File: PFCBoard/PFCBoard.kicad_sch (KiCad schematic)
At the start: 17 parts, among them J1 VIN 10-30VDC, J2 Coin Out, U1 NE555D, U2 MC78L05_SOT89, U3 LTV-817S

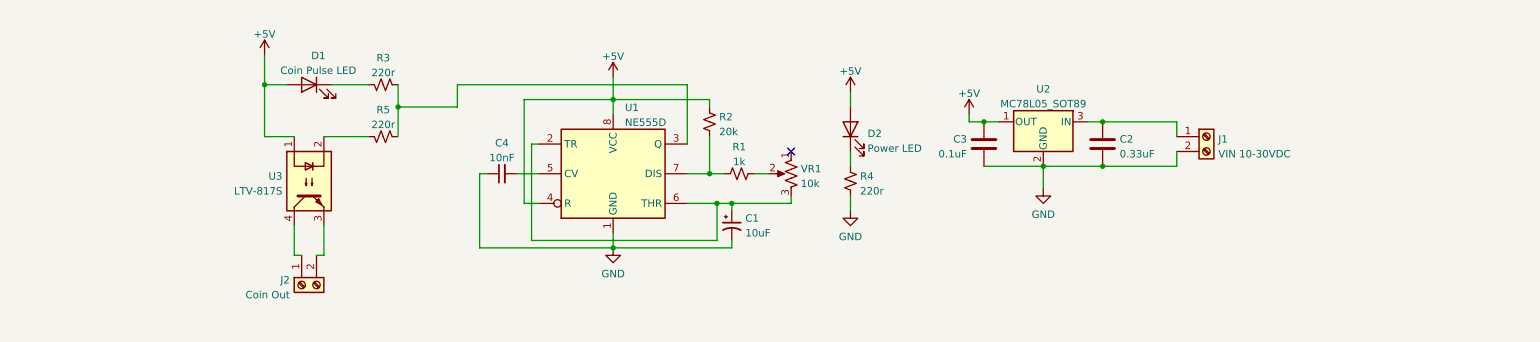
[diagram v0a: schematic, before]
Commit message: Add voltage selection, pre-rendered schematic
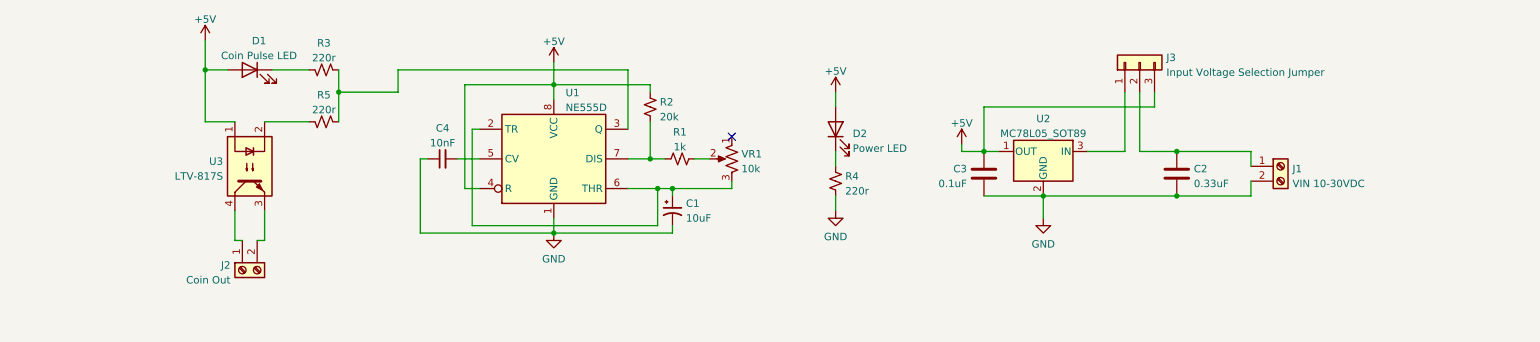
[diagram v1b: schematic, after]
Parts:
- added J3: Input Voltage Selection Jumper, symbol Connector_Generic:Conn_01x03
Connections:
- net +5V: now also J3.3 (Pin_3)
- net at C2.1, J1.1 (Pin_1): now also J3.2 (Pin_2); no longer U2.3 (IN)
- new net: J3.1 (Pin_1), U2.3 (IN)
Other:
- moved on the sheet: C1, C2, C3, C4, D1, D2, J1, J2, R1, R2, R3, R4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

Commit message: PCB design, schematic/readme tweaks
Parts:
- removed J1: VIN 10-30VDC, symbol Connector:Screw_Terminal_01x02
- removed J2: Coin Out, symbol Connector:Screw_Terminal_01x02
- removed J3: Input Voltage Selection Jumper, symbol Connector_Generic:Conn_01x03
- added H1, H2, H3, H4: MountingHole, MountingHole:MountingHole_3mm, symbol Mechanical:MountingHole
- added J1: VIN 10-30VDC, 1713017, symbol 1713017:1713017
- added J2: Coin Out, 1713017, symbol 1713017:1713017
- added JP1: 5V Reg. Bypass, Jumper:SolderJumper-3_P1.3mm_Bridged12_Pad1.0x1.5mm, symbol Jumper:SolderJumper_3_Bridged12
- added JP2: 5V Reg. Enable, Jumper:SolderJumper-2_P1.3mm_Bridged_Pad1.0x1.5mm, symbol Jumper:SolderJumper_2_Bridged
- C1: footprint (none) -> Capacitor_SMD:CP_Elec_4x4.5
- C2, C3, C4: footprint (none) -> Capacitor_SMD:C_1206_3216Metric_Pad1.33x1.80mm_HandSolder
- D1: value Coin Pulse LED -> Coin Pulse; footprint (none) -> LED_SMD:LED_1206_3216Metric_Pad1.42x1.75mm_HandSolder
- D2: value Power LED -> Power; footprint (none) -> LED_SMD:LED_1206_3216Metric_Pad1.42x1.75mm_HandSolder
- R1, R2: footprint (none) -> Resistor_SMD:R_1206_3216Metric_Pad1.30x1.75mm_HandSolder
- R3, R4, R5: value 220r -> 330r; footprint (none) -> Resistor_SMD:R_1206_3216Metric_Pad1.30x1.75mm_HandSolder
- VR1: footprint (none) -> Potentiometer_SMD:Potentiometer_Bourns_TC33X_Vertical
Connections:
- net +5V: now also JP1.3 (B), JP2.1 (A); no longer U2.1 (OUT)
- net GND: now also J1.2
- net at U3.3: now also J2.2
- net at U3.4: now also J2.1
- net at U2.3 (IN): now also JP1.1 (A)
- net at C2.1: now also J1.1, JP1.2 (C)
- new net: JP2.2 (B), U2.1 (OUT)
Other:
- moved on the sheet: C1, C2, C3, C4, D1, D2, R1, R2, R3, R4, R5, U1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
